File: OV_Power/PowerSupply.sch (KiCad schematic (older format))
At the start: 15 parts, among them J1 Kycon_kpjx-4s, J2 Conn_HDR_2x10_latching, J3 532530670, J6 CONN_HEADER_2.54X2_MOLEX_KK_S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, J7 CONN_HEADER_2.54X2_MOLEX_KK_S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, Q3 SZNUD3124LT1G, Q4 SZNUD3124LT1G, U7 LTC4416, U8 AOSD21307, U9 AOSD21307

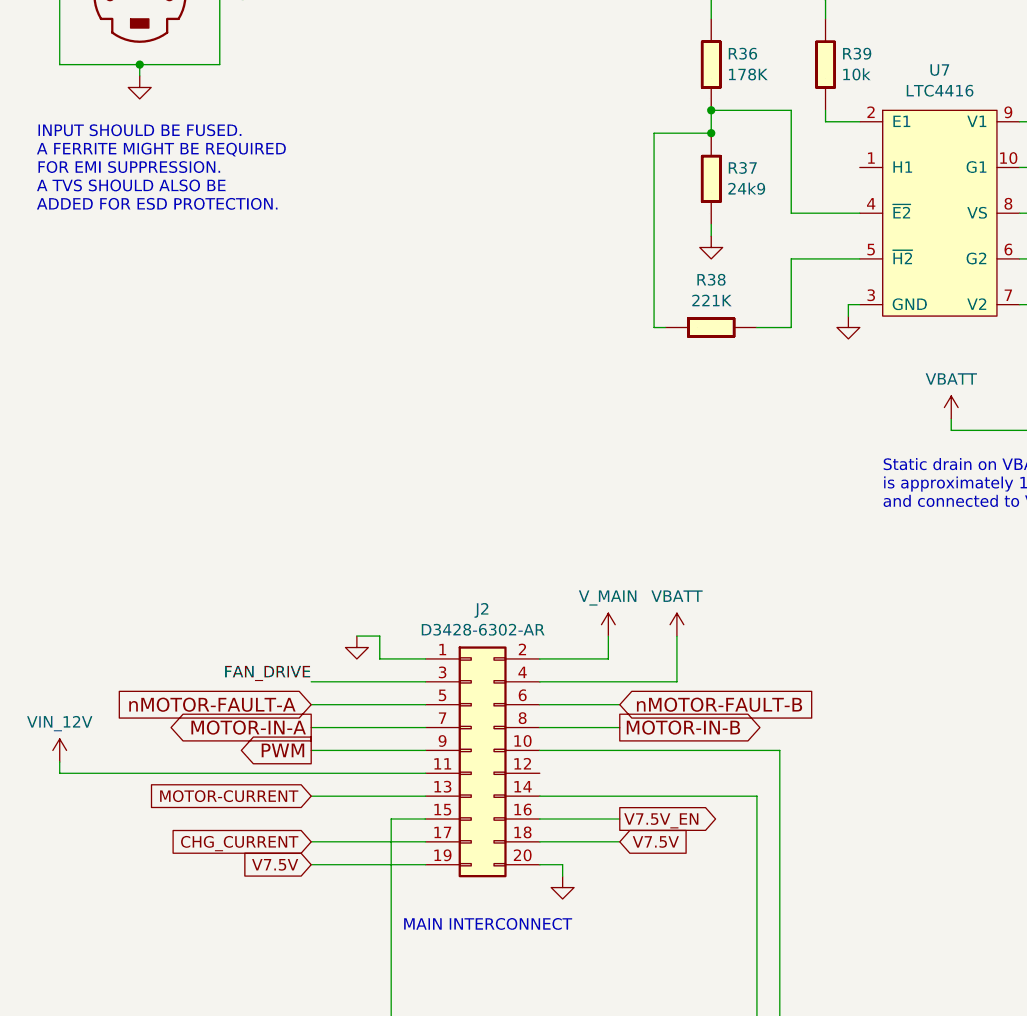
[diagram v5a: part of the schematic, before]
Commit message: Finished schemo and placement of power supply board, then resolved interconnects with the main board.
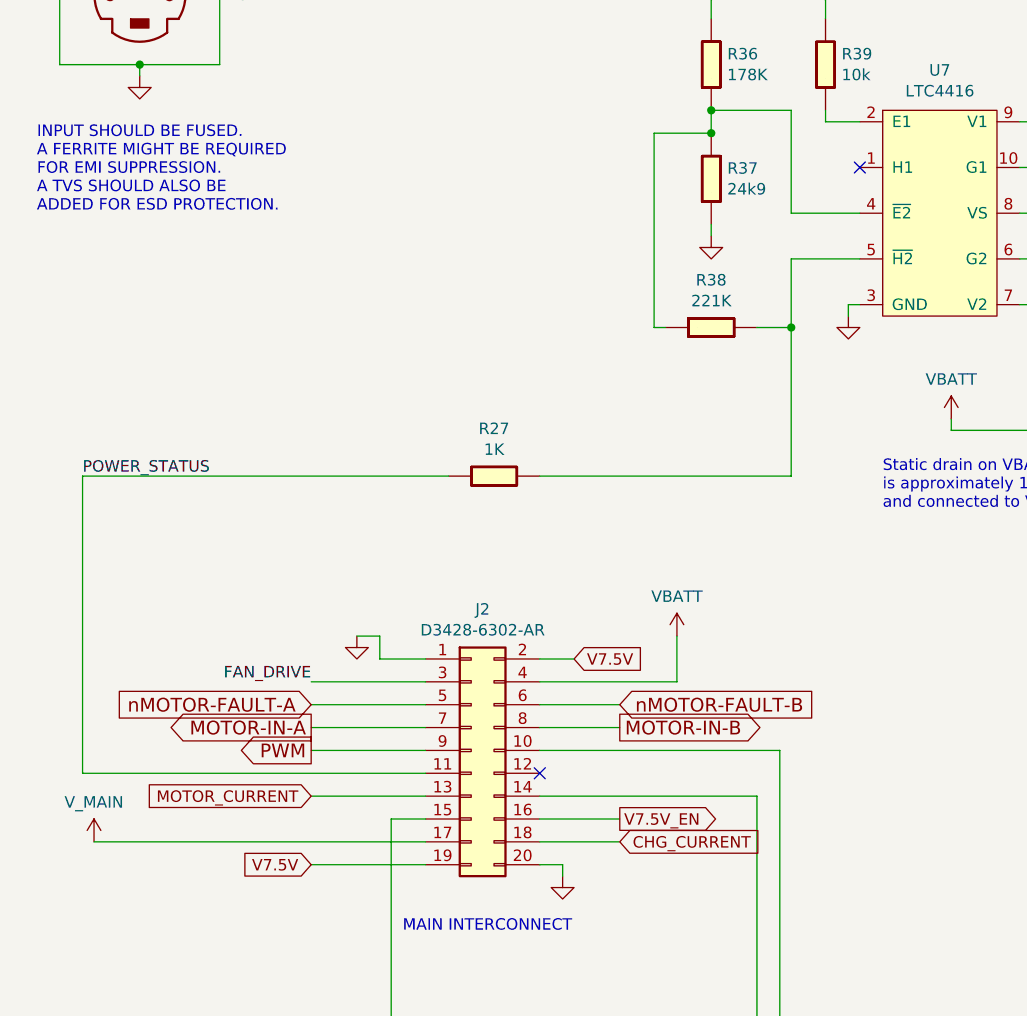
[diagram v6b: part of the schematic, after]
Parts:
- added R27: 1K_0603_Chip_Resistor,_1%,_0.1W, Resistor_SMD:R_0603_1608Metric, symbol OpenVent:1K_0603_Chip_Resistor,_1%,_0.1W
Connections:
- net CHG_CURRENT: now also J2.18 (Pin_18); no longer J2.17 (Pin_17)
- net V7.5V: now also J2.2 (Pin_2); no longer J2.18 (Pin_18)
- net V_MAIN: now also J2.17 (Pin_17); no longer J2.2 (Pin_2)
- net at R38.1, U7.5 (~H2~): now also R27.2
- net MOTOR-CURRENT renamed MOTOR_CURRENT
- net VIN_12V renamed POWER_STATUS
- net POWER_STATUS: now also R27.1
- no-connect marks 0 -> 2
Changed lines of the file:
@@
 L OpenVent:V_MAIN #PWR031
 U 1 1 5FB4FD2E
-P 3100 4500
-F 0 "#PWR031" H 3100 4350 50  0001 C CNN
-F 1 "V_MAIN" H 3100 4673 50  0000 C CNN
-F 2 "" H 3100 4500 50  0001 C CNN
-F 3 "" H 3100 4500 50  0001 C CNN
-	1    3100 4500
+P 850 5400
+F 0 "#PWR031" H 850 5250 50  0001 C CNN
+F 1 "V_MAIN" H 850 5573 50  0000 C CNN
+F 2 "" H 850 5400 50  0001 C CNN
+F 3 "" H 850 5400 50  0001 C CNN
+	1    850  5400
 	1    0    0    -1
 $EndComp
 Text GLabel 1800 5500 0    50   Input ~ 0
 V7.5V
-Text GLabel 3150 5400 2    50   Input ~ 0
+Text GLabel 2950 4600 2    50   Input ~ 0
 V7.5V
 Text GLabel 3150 5300 2    50   Output ~ 0
@@
 	2100 4500 2000 4500
 Wire Wire Line
-	2800 4600 3100 4600
-Wire Wire Line
-	3100 4600 3100 4500
-Wire Wire Line
 	2300 5500 1800 5500
-Wire Wire Line
-	3150 5400 2800 5400
 Wire Wire Line
 	3150 5300 2800 5300
@@
 Wire Wire Line
 	2300 5000 1800 5000
-Text GLabel 1800 5400 0    50   Input ~ 0
+Text GLabel 3150 5400 2    50   Input ~ 0
 CHG_CURRENT
-Wire Wire Line
-	2300 5400 1800 5400
-$Comp
-L OpenVent:VIN_12V #PWR017
-U 1 1 5FBA1DE1
-P 700 5050
-F 0 "#PWR017" H 700 4900 50  0001 C CNN
-F 1 "VIN_12V" H 700 5223 50  0000 C CNN
-F 2 "" H 700 5050 60  0001 C CNN
-F 3 "" H 700 5050 60  0001 C CNN
-	1    700  5050
-	1    0    0    -1
-$EndComp
-Wire Wire Line
-	2300 5100 700  5100
-Wire Wire Line
-	700  5100 700  5050
 Text GLabel 1800 5200 0    50   Input ~ 0
-MOTOR-CURRENT
+MOTOR_CURRENT
 Wire Wire Line
 	2300 5200 1800 5200
@@
 Connection ~ 1500 1700
 Connection ~ 3550 1700
+$Comp
+L OpenVent:1K_0603_Chip_Resistor,_1%,_0.1W R27
+U 1 1 5FD89289
+P 2500 3700
+F 0 "R27" H 2600 3807 50  0000 C CNN
+F 1 "1K_0603_Chip_Resistor,_1%,_0.1W" H 2500 3700 50  0001 C CNN
+F 2 "Resistor_SMD:R_0603_1608Metric" H 2500 3700 60  0001 C CNN
+F 3 "" H 2500 3700 60  0001 C CNN
+F 4 "1K" H 2600 3716 50  0000 C CNN "Val"
+F 5 "1%" H 2500 3700 50  0001 C CNN "Tolerance"
+F 6 "0.1W" H 2500 3700 50  0001 C CNN "Watt"
+	1    2500 3700
+	1    0    0    -1
+$EndComp
+Wire Wire Line
+	3900 3150 3900 3800
+Wire Wire Line
+	3900 3800 2800 3800
+Connection ~ 3900 3150
+Wire Wire Line
+	2400 3800 800  3800
+Wire Wire Line
+	800  3800 800  5100
+Wire Wire Line
+	800  5100 2300 5100
+Text Label 800  3800 0    50   ~ 0
+POWER_STATUS
+Wire Wire Line
+	2950 4600 2800 4600
+Wire Wire Line
+	2300 5400 850  5400
+Wire Wire Line
+	3150 5400 2800 5400
+NoConn ~ 4200 2450
+NoConn ~ 2800 5100
 $EndSCHEMATC

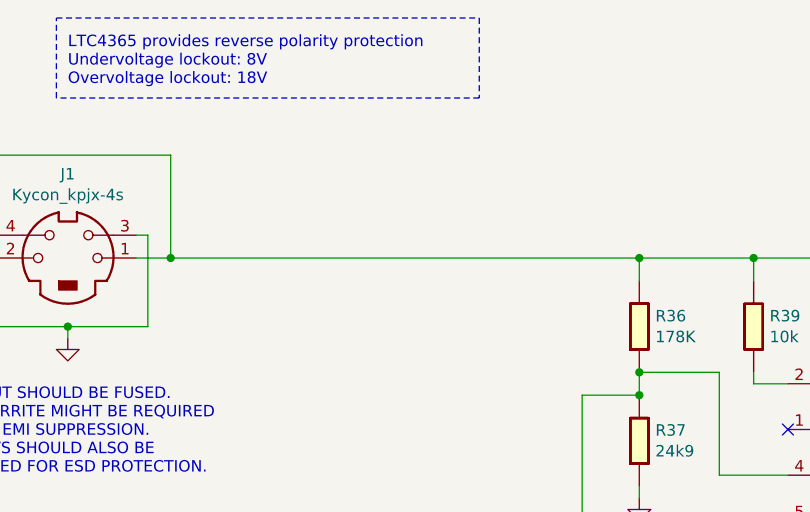
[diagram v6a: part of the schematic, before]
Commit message: First cut at complete routing for the power board.  Still need DRC checking and final fettling of the BOM and silkscreens before going to press.
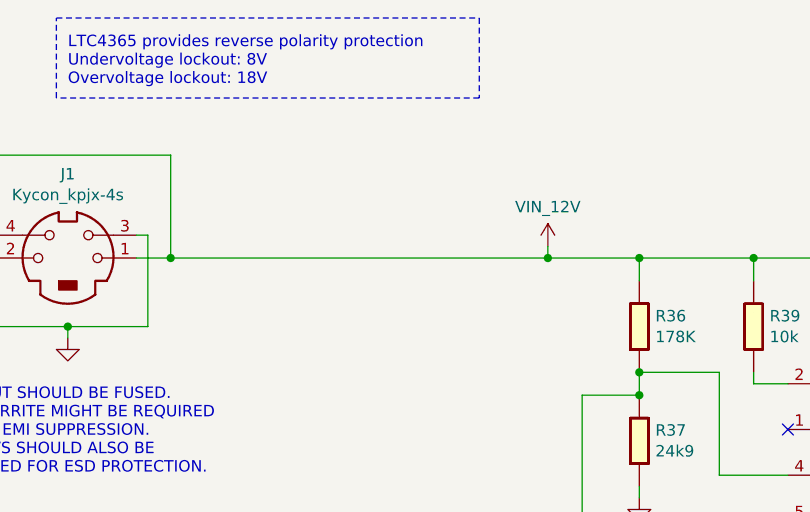
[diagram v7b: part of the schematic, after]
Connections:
- net VIN_12V: now reaches J1.1, J1.4, R36.1, R39.1, U7.9 (V1), U8.1 (S)
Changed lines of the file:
@@
 FAN_DRIVE
 Wire Wire Line
-	1500 1700 3550 1700
+	1500 1700 3150 1700
 Connection ~ 1500 1700
 Connection ~ 3550 1700
@@
 NoConn ~ 4200 2450
 NoConn ~ 2800 5100
+$Comp
+L OpenVent:VIN_12V #PWR0101
+U 1 1 5FDCF50B
+P 3150 1650
+F 0 "#PWR0101" H 3150 1500 50  0001 C CNN
+F 1 "VIN_12V" H 3150 1823 50  0000 C CNN
+F 2 "" H 3150 1650 60  0001 C CNN
+F 3 "" H 3150 1650 60  0001 C CNN
+	1    3150 1650
+	1    0    0    -1
+$EndComp
+Wire Wire Line
+	3150 1650 3150 1700
+Connection ~ 3150 1700
+Wire Wire Line
+	3150 1700 3550 1700
 $EndSCHEMATC

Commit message: Changed the power input jack to a shielded version of the same part. Note that the same footprint can be used with either shielded or unshielded versions.
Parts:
- J1: value Kycon_kpjx-4s -> Kycon_kpjx-4s_shielded; footprint OpenVent:Kycon_KPJX-4S -> OpenVent:Kycon_KPJX-4S_SHIELD; symbol OpenVent:Kycon_kpjx-4s -> OpenVent:Kycon_kpjx-4s_shielded; Mfr_PN KPJX-4S -> KPJX-4S-S
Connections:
- net GND: now also J1.5, J1.6, J1.7, J1.8
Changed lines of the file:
@@
 	2300 5200 1800 5200
 $Comp
-L OpenVent:Kycon_kpjx-4s J1
+L OpenVent:Kycon_kpjx-4s_shielded J1
 U 1 1 5FBCEB95
 P 1050 1700
 F 0 "J1" H 1050 2067 50  0000 C CNN
-F 1 "Kycon_kpjx-4s" H 1050 1976 50  0000 C CNN
-F 2 "OpenVent:Kycon_KPJX-4S" H 1050 1700 50  0001 C CNN
-F 3 "http://www.kycon.com/Pub_Eng_Draw/KPJX-4S.pdf" H 1050 1700 50  0001 C CNN
+F 1 "Kycon_kpjx-4s_shielded" H 1100 2250 50  0000 C CNN
+F 2 "OpenVent:Kycon_KPJX-4S_SHIELD" H 1050 1700 50  0001 C CNN
+F 3 "http://www.kycon.com/Pub_Eng_Draw/KPJX-4S-S.pdf" H 1050 1700 50  0001 C CNN
 F 4 "Kycon, Inc." H 1050 1700 50  0001 C CNN "Mfr"
-F 5 "KPJX-4S" H 1050 1700 50  0001 C CNN "Mfr_PN"
+F 5 "KPJX-4S-S" H 1050 1700 50  0001 C CNN "Mfr_PN"
 F 6 "4 (Power) Position Circular Connector Jack, Female Sockets Solder" H 1050 1700 50  0001 C CNN "Detailed"
 F 7 "CONN JACK FMALE 4POS TIN SOLDER" H 1050 1700 50  0001 C CNN "Desc"
@@
 	1350 1600 1400 1600
 Wire Wire Line
-	1400 1600 1400 2000
+	1400 1600 1400 1800
 Wire Wire Line
 	1400 2000 1050 2000
 Wire Wire Line
-	700  2000 700  1700
+	700  2000 700  1900
 Wire Wire Line
 	700  1700 750  1700
@@
 Wire Wire Line
 	3150 1700 3550 1700
+Wire Wire Line
+	750  1800 700  1800
+Connection ~ 700  1800
+Wire Wire Line
+	700  1800 700  1700
+Wire Wire Line
+	750  1900 700  1900
+Connection ~ 700  1900
+Wire Wire Line
+	700  1900 700  1800
+Wire Wire Line
+	1350 1900 1400 1900
+Connection ~ 1400 1900
+Wire Wire Line
+	1400 1900 1400 2000
+Wire Wire Line
+	1350 1800 1400 1800
+Connection ~ 1400 1800
+Wire Wire Line
+	1400 1800 1400 1900
 $EndSCHEMATC
